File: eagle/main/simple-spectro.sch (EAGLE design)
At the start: 54 parts, among them CON1 BAT, CON2 SPI, CON3 SPI, CON4 VIBR, IC1 32U4, IC2 MCP73831T, IC3 MCP1703-33, IC4 DMP1045U or DMG2302, Q6 BSP75, U1 TMP75DGK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

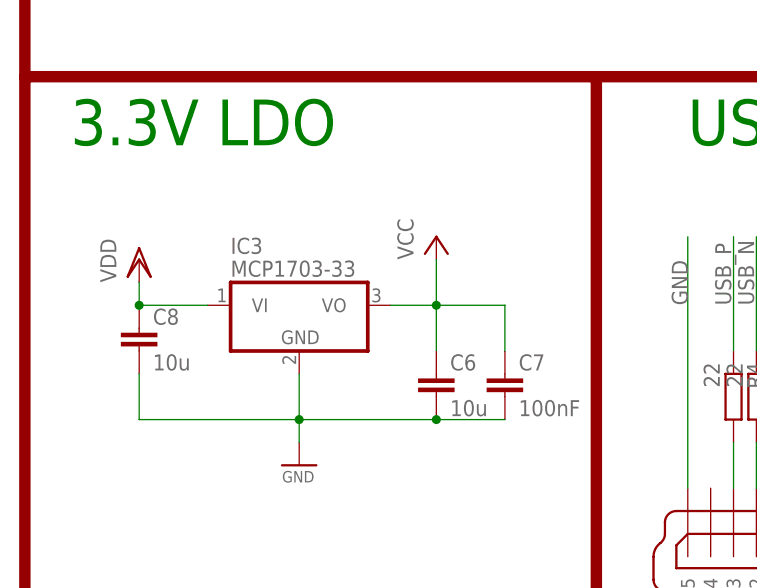
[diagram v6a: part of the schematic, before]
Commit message: final design for price quote 1206 elecrow
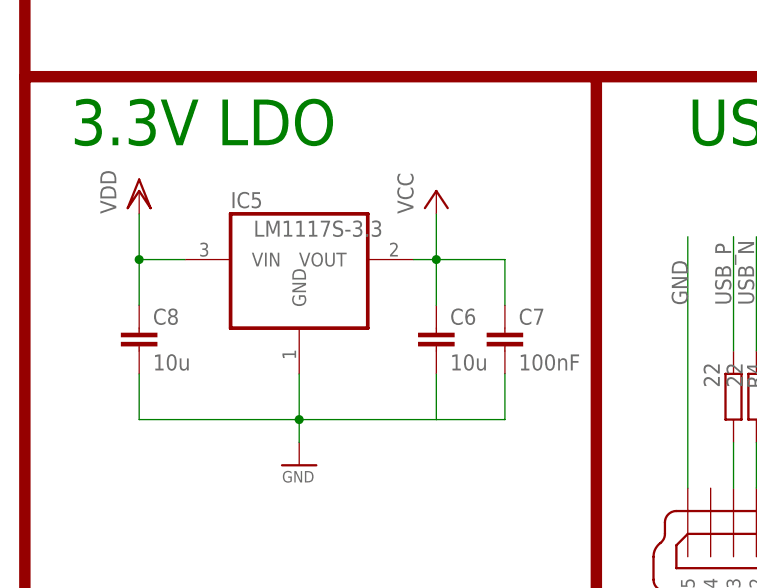
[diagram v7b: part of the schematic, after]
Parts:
- removed IC3: MCP1703-33, linear:MCP1703DB
- added IC5: LM1117S-3.3, burr-brown:REG1117
- Q6: LCSC (none) -> C111029
- R12: ELECROW C26124 -> (none); LCSC (none) -> C26124
- X1: LCSC C90881 -> C122522
- X2: LCSC (none) -> C46391
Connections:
- net GND: now also IC5.GND; no longer IC3.GND
- net VCC: now also IC5.VOUT; no longer IC3.VO
- net VDD: now also IC5.VIN; no longer IC3.VI
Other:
- moved on the sheet: C6, C7
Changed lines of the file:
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@@
 <schematic xreflabel="%F%N/%S.%C%R" xrefpart="/%S.%C%R">
 <attributes>
+<attribute name="DELETE" value="MF"/>
 </attributes>
 <variantdefs>
@@
 </part>
 <part name="X2" library="con-cypressindustries" deviceset="MINI-USB-SCHIELD-" device="32005-201" value="MINI-USB">
+<attribute name="LCSC" value="C46391"/>
 <attribute name="MPN" value="649-10033526-N3212LF"/>
 <attribute name="OC_FARNELL" value=""/>
@@
 </part>
 <part name="X1" library="lpatiny" deviceset="XTAL" device="NX6035" value="8MHz">
-<attribute name="LCSC" value="C90881"/>
+<attribute name="LCSC" value="C122522"/>
 <attribute name="MPN" value="729-F60800010"/>
 </part>
@@
 <part name="GND54" library="supply1" deviceset="GND" device=""/>
 <part name="R12" library="rcl" library_urn="urn:adsk.eagle:library:334" deviceset="R-EU_" device="M1206" value="1M">
-<attribute name="ELECROW" value="C26124"/>
+<attribute name="ELECROW" value=""/>
+<attribute name="LCSC" value="C26124"/>
 <attribute name="MPN" value="ERJ-8GEYJ105V"/>
 </part>
@@
 <attribute name="MPN" value="77-VJ1206V106ZXQTBC"/>
 </part>
-<part name="IC3" library="linear" deviceset="MCP1703" device="DB" value="MCP1703-33">
-<attribute name="LCSC" value="C50754"/>
-<attribute name="MPN" value="579-MCP1703-3302E/DB"/>
-</part>
 <part name="SUPPLY3" library="supply1" deviceset="VDD" device=""/>
 <part name="P+1" library="supply1" deviceset="VCC" device=""/>
@@
 <attribute name="MPN" value="667-ERJ-8GEYJ101V"/>
 </part>
-<part name="Q6" library="infineon" deviceset="BSP613P" device="" value="BSP75"/>
+<part name="Q6" library="infineon" deviceset="BSP613P" device="" value="BSP75">
+<attribute name="LCSC" value="C111029"/>
+</part>
 <part name="GND12" library="supply1" deviceset="GND" device=""/>
 <part name="SUPPLY10" library="supply1" deviceset="VCC" device=""/>
+<part name="IC5" library="burr-brown" library_urn="urn:adsk.eagle:library:111" deviceset="REG1117" device="" package3d_urn="urn:adsk.eagle:package:4940/1" value="LM1117S-3.3">
+<attribute name="LCSC" value="C126027"/>
+</part>
 </parts>
 <sheets>
@@
 <attribute name="ELECROW" x="93.98" y="121.92" size="1.778" layer="96" rot="MR180" display="off"/>
 </instance>
-<instance part="X2" gate="G$1" x="63.5" y="17.78" rot="R270"/>
+<instance part="X2" gate="G$1" x="63.5" y="17.78" rot="R270">
+<attribute name="LCSC" x="63.5" y="17.78" size="1.778" layer="96" rot="R270" display="off"/>
+</instance>
 <instance part="R4" gate="G$1" x="63.5" y="33.02" rot="R270">
 <attribute name="MPN" x="63.5" y="33.02" size="1.778" layer="96" rot="R270" display="off"/>
@@
 <attribute name="MPN" x="96.52" y="165.1" size="1.778" layer="96" rot="MR90" display="off"/>
 <attribute name="ELECROW" x="96.52" y="165.1" size="1.778" layer="96" rot="MR90" display="off"/>
+<attribute name="LCSC" x="96.52" y="165.1" size="1.778" layer="96" rot="MR90" display="off"/>
 </instance>
 <instance part="SUPPLY18" gate="VCC" x="96.52" y="203.2"/>
@@
 <attribute name="VALUE" x="13.335" y="23.495" size="1.27" layer="96"/>
 </instance>
-<instance part="C6" gate="G$1" x="30.48" y="35.56">
-<attribute name="MPN" x="30.48" y="35.56" size="1.778" layer="96" display="off"/>
-<attribute name="LCSC" x="30.48" y="35.56" size="1.778" layer="96" display="off"/>
-<attribute name="ELECROW" x="30.48" y="35.56" size="1.778" layer="96" display="off"/>
-</instance>
-<instance part="IC3" gate="G$1" x="15.24" y="43.18">
-<attribute name="MPN" x="15.24" y="43.18" size="1.778" layer="96" display="off"/>
-<attribute name="LCSC" x="15.24" y="43.18" size="1.778" layer="96" display="off"/>
-</instance>
-<instance part="SUPPLY3" gate="G$1" x="-2.54" y="48.26"/>
-<instance part="P+1" gate="VCC" x="30.48" y="50.8"/>
+<instance part="C6" gate="G$1" x="30.48" y="40.64">
+<attribute name="MPN" x="30.48" y="40.64" size="1.778" layer="96" display="off"/>
+<attribute name="LCSC" x="30.48" y="40.64" size="1.778" layer="96" display="off"/>
+<attribute name="ELECROW" x="30.48" y="40.64" size="1.778" layer="96" display="off"/>
+</instance>
+<instance part="SUPPLY3" gate="G$1" x="-2.54" y="55.88"/>
+<instance part="P+1" gate="VCC" x="30.48" y="55.88"/>
 <instance part="IC4" gate="G$1" x="157.48" y="104.14" rot="MR270">
 <attribute name="MPN" x="157.48" y="104.14" size="1.778" layer="96" rot="MR270" display="off"/>
@@
 <attribute name="LCSC" x="20.32" y="86.36" size="1.778" layer="96" display="off"/>
 </instance>
-<instance part="C7" gate="G$1" x="38.1" y="35.56">
-<attribute name="MPN" x="38.1" y="35.56" size="1.778" layer="96" display="off"/>
-<attribute name="LCSC" x="38.1" y="35.56" size="1.778" layer="96" display="off"/>
-<attribute name="ELECROW" x="38.1" y="35.56" size="1.778" layer="96" display="off"/>
+<instance part="C7" gate="G$1" x="38.1" y="40.64">
+<attribute name="MPN" x="38.1" y="40.64" size="1.778" layer="96" display="off"/>
+<attribute name="LCSC" x="38.1" y="40.64" size="1.778" layer="96" display="off"/>
+<attribute name="ELECROW" x="38.1" y="40.64" size="1.778" layer="96" display="off"/>
 </instance>
 <instance part="R11" gate="G$1" x="83.82" y="215.9" rot="R180">
@@
 <attribute name="ELECROW" x="12.7" y="144.78" size="1.778" layer="96" display="off"/>
 </instance>
-<instance part="Q6" gate="G$1" x="27.94" y="147.32"/>
+<instance part="Q6" gate="G$1" x="27.94" y="147.32">
+<attribute name="LCSC" x="27.94" y="147.32" size="1.778" layer="96" display="off"/>
+</instance>
 <instance part="GND12" gate="1" x="30.48" y="137.16" rot="MR0"/>
 <instance part="SUPPLY10" gate="VCC" x="30.48" y="162.56"/>
+<instance part="IC5" gate="G$1" x="15.24" y="48.26">
+<attribute name="LCSC" x="15.24" y="48.26" size="1.778" layer="96" display="off"/>
+</instance>
 </instances>
 <busses>
@@
 <wire x1="-2.54" y1="35.56" x2="-2.54" y2="30.48" width="0.1524" layer="91"/>
 <wire x1="-2.54" y1="30.48" x2="15.24" y2="30.48" width="0.1524" layer="91"/>
-<wire x1="15.24" y1="30.48" x2="30.48" y2="30.48" width="0.1524" layer="91"/>
 <pinref part="GND19" gate="1" pin="GND"/>
 <pinref part="C8" gate="G$1" pin="2"/>
@@
 <pinref part="C6" gate="G$1" pin="2"/>
 <wire x1="15.24" y1="30.48" x2="15.24" y2="35.56" width="0.1524" layer="91"/>
-<pinref part="IC3" gate="G$1" pin="GND"/>
 <pinref part="C7" gate="G$1" pin="2"/>
+<pinref part="IC5" gate="G$1" pin="GND"/>
+<wire x1="15.24" y1="30.48" x2="30.48" y2="30.48" width="0.1524" layer="91"/>
+<wire x1="30.48" y1="35.56" x2="30.48" y2="30.48" width="0.1524" layer="91"/>
 <wire x1="30.48" y1="30.48" x2="38.1" y2="30.48" width="0.1524" layer="91"/>
-<junction x="30.48" y="30.48"/>
+<wire x1="38.1" y1="30.48" x2="38.1" y2="35.56" width="0.1524" layer="91"/>
 </segment>
 <segment>
@@
 <pinref part="C8" gate="G$1" pin="1"/>
 <pinref part="SUPPLY3" gate="G$1" pin="VDD"/>
-<wire x1="-2.54" y1="45.72" x2="-2.54" y2="43.18" width="0.1524" layer="91"/>
-<pinref part="IC3" gate="G$1" pin="VI"/>
-<wire x1="5.08" y1="43.18" x2="-2.54" y2="43.18" width="0.1524" layer="91"/>
-<junction x="-2.54" y="43.18"/>
+<wire x1="-2.54" y1="53.34" x2="-2.54" y2="48.26" width="0.1524" layer="91"/>
+<pinref part="IC5" gate="G$1" pin="VIN"/>
+<wire x1="-2.54" y1="48.26" x2="-2.54" y2="43.18" width="0.1524" layer="91"/>
+<wire x1="2.54" y1="48.26" x2="-2.54" y2="48.26" width="0.1524" layer="91"/>
+<junction x="-2.54" y="48.26"/>
 </segment>
 <segment>
@@
 <net name="VCC" class="0">
 <segment>
-<wire x1="30.48" y1="43.18" x2="30.48" y2="38.1" width="0.1524" layer="91"/>
-<junction x="30.48" y="43.18"/>
+<wire x1="30.48" y1="48.26" x2="30.48" y2="43.18" width="0.1524" layer="91"/>
+<junction x="30.48" y="48.26"/>
 <pinref part="C6" gate="G$1" pin="1"/>
-<wire x1="25.4" y1="43.18" x2="30.48" y2="43.18" width="0.1524" layer="91"/>
-<pinref part="IC3" gate="G$1" pin="VO"/>
 <pinref part="P+1" gate="VCC" pin="VCC"/>
-<wire x1="30.48" y1="43.18" x2="30.48" y2="48.26" width="0.1524" layer="91"/>
+<wire x1="27.94" y1="48.26" x2="30.48" y2="48.26" width="0.1524" layer="91"/>
+<wire x1="30.48" y1="48.26" x2="30.48" y2="53.34" width="0.1524" layer="91"/>
 <pinref part="C7" gate="G$1" pin="1"/>
-<wire x1="38.1" y1="38.1" x2="38.1" y2="43.18" width="0.1524" layer="91"/>
-<wire x1="30.48" y1="43.18" x2="38.1" y2="43.18" width="0.1524" layer="91"/>
-</segment>
-<segment>
+<wire x1="38.1" y1="43.18" x2="38.1" y2="48.26" width="0.1524" layer="91"/>
+<wire x1="30.48" y1="48.26" x2="38.1" y2="48.26" width="0.1524" layer="91"/>
+<pinref part="IC5" gate="G$1" pin="VOUT"/>
+</segment>
+<segment>

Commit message: work on 0805
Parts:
- C1, C2: device resistor:C-EUC1206 -> rcl:C-EUC0805K; ELECROW (none) -> C1797; LCSC C1889 -> C1797
- C10, C3, C9: device resistor:C-EUC1206 -> rcl:C-EUC0805K; ELECROW C24497 -> C49678; LCSC C77502 -> C49678
- C4, C5: device dp_devices:CAPACITOR_NPOL-1206 -> rcl:C-EUC0805K; ELECROW C13585 -> C15850; LCSC C92789 -> C15850
- C6, C8: device resistor:C-EUC1206 -> rcl:C-EUC0805K; ELECROW C13585 -> C15850; LCSC C92789 -> C15850
- C7: device resistor:C-EUC1206 -> rcl:C-EUC0805K; ELECROW C24497 -> C49678
- R1, R14, R2, R20, R7, R8, R9: device rcl:R-EU_M1206 -> rcl:R-EU_R0805; ELECROW C4410 -> C17513; LCSC C1469 -> C17513; MPN 667-ERJ-8GEYJ101V -> (none)
- R10: device rcl:R-EU_M1206 -> rcl:R-EU_R0805; ELECROW (none) -> C17557; LCSC C102128 -> C17557; MPN 667-ERJ-U08J221V -> (none)
- R11, R15: device rcl:R-EU_M1206 -> rcl:R-EU_R0805; ELECROW C17900 -> C118844; LCSC C17900 -> C118844
- R12: device rcl:R-EU_M1206 -> rcl:R-EU_R0805; ELECROW (none) -> C17514; LCSC C26124 -> C17514; MPN ERJ-8GEYJ105V -> (none)
- R13, R3: device rcl:R-EU_M1206 -> rcl:R-EU_R0805; ELECROW C17902 -> C17414; LCSC C17902 -> C17414; MPN 603-RC1206FR-0710KL -> (none)
- R16, R17, R18, R19: device rcl:R-EU_M1206 -> rcl:R-EU_R0805; ELECROW C17900 -> C17414; LCSC C17900 -> C17414; MPN 603-RC1206FR-0710KL -> (none)
- R4, R5: device rcl:R-EU_M1206 -> rcl:R-EU_R0805; ELECROW C17958 -> C17561; LCSC C99734 -> C17561; MPN 603-RC1206FR-0722RL -> (none)
- R6: device rcl:R-EU_M1206 -> rcl:R-EU_R0805; ELECROW (none) -> C17408; LCSC C4410 -> C17408
